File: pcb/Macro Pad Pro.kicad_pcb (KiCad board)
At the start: 4 copper layers, 107 x 134 mm, 150 parts, among them J1 USB_C, J2 Conn_02x08_Odd_Even, J3 Conn_02x01, J4 Conn_02x01, SW1 SW_Push_B, SW2 SW_Push_R, U1 RP2040, U3 AP2112K-3.3, U4 USBLC6-2SC6, U6 W25Q128JVS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

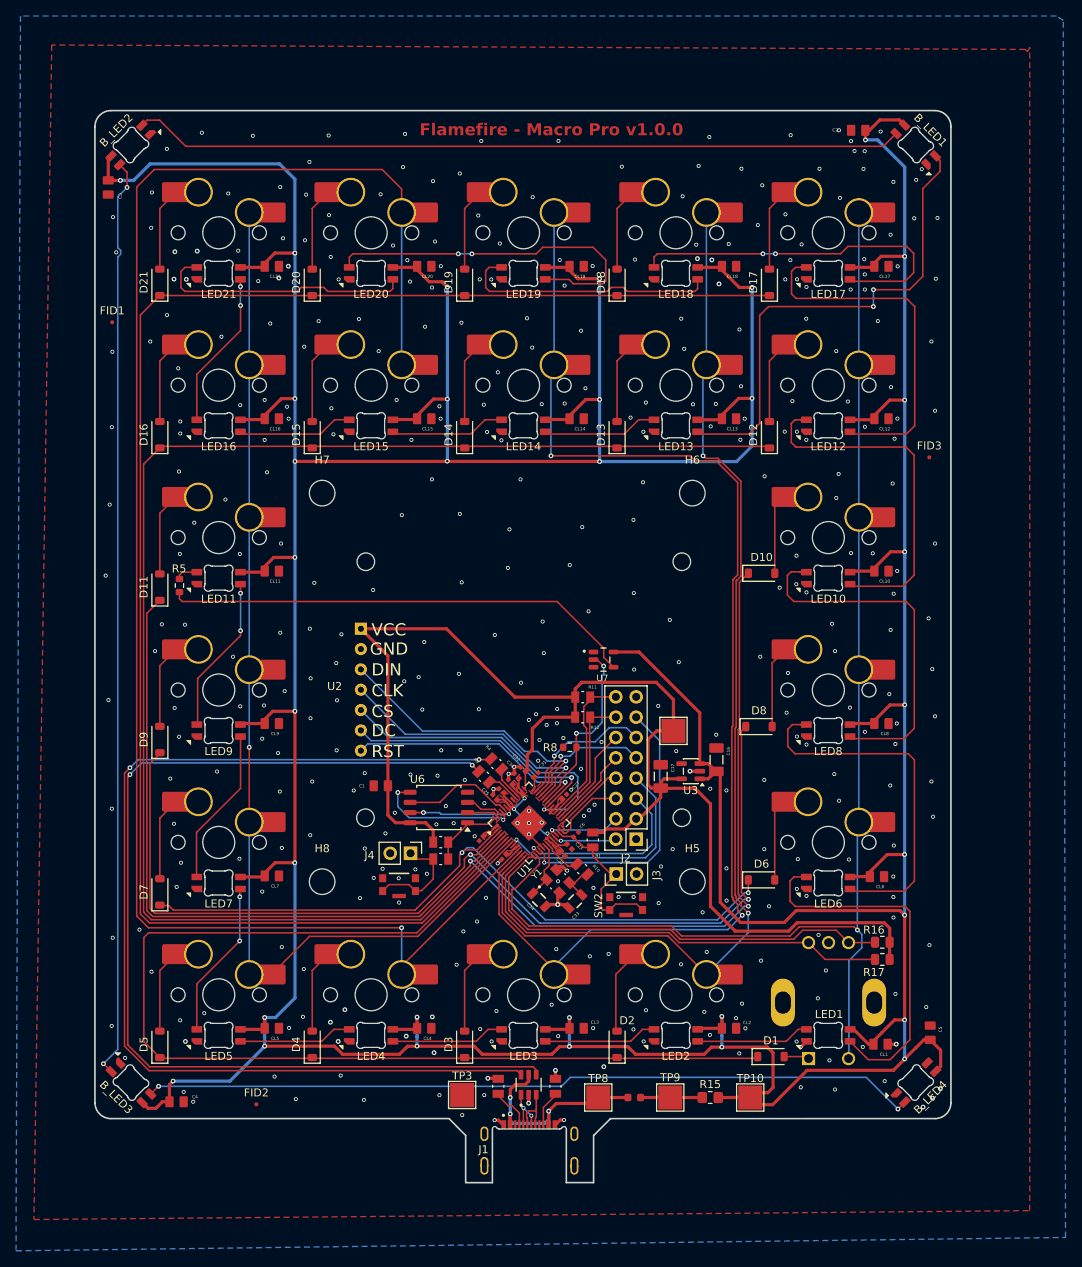
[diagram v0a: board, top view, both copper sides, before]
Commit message: cleaned up BOM and updated most components with LCSC number and MPN, sent to PCBWay for review
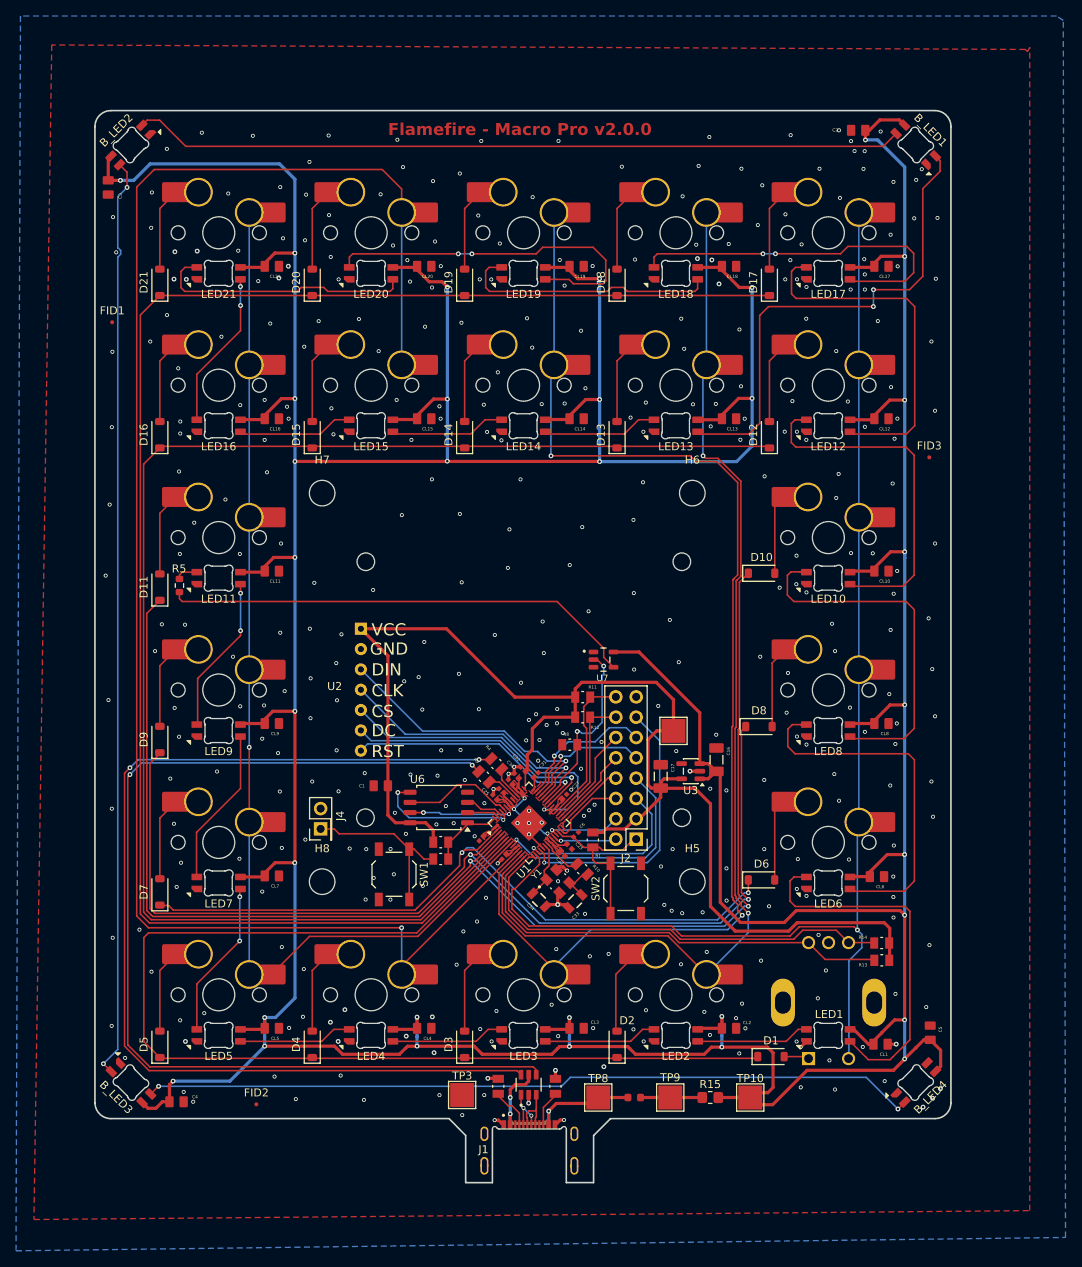
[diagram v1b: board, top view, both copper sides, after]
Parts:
- removed J3: Conn_02x01, Connector_PinHeader_2.54mm:PinHeader_1x02_P2.54mm_Vertical
- removed R16, R17: 10k, Resistor_SMD:R_0805_2012Metric
- added R13: 10k, Personal:10k_RESC2012X65N, F.Cu at (139.8, 154.7)
- added R14: 10k, Personal:10k_RESC2012X65N, F.Cu at (139.8, 152.5)
- J4: footprint Connector_PinHeader_2.54mm:PinHeader_1x02_P2.54mm_Vertical -> Connector_PinHeader_2.54mm:PinHeader_2x01_P2.54mm_Vertical
- R5: value 500 ohm -> 470 ohm
- R8: value 500 ohm -> 10k; footprint Resistor_SMD:R_0603_1608Metric -> Personal:10k_RESC2012X65N
- SW1, SW2: footprint Personal:SW_KMR221GLFS -> Button_Switch_SMD:SW_SPST_TL3342
- U1: footprint Personal:QFN-56-1EP_7x7mm_P0.4mm_EP3.2x3.2mm -> Package_DFN_QFN:QFN-56-1EP_7x7mm_P0.4mm_EP3.2x3.2mm
- U2: value ~ -> OLED
- moved J4 11.6 mm to (69.7, 138.2), turned to 90 degrees
- moved SW2 1.89 mm to (107.8, 145.7), turned to 90 degrees
- moved SW1 1.44 mm to (78.9, 143.9), turned to -90 degrees
- moved R8 0.32 mm to (100.8, 127.7)
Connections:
- J2 pad 1: unconnected-(J2-Pin_1-Pad1) -> NRST
- J2 pad 15: unconnected-(J2-Pin_15-Pad15) -> GND
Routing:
- net BOOTSEL: track 13.2 -> 21.9 mm
- net NRST: track 21.0 -> 21.6 mm
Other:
- copper layers 4 -> 2
- board text added: "Flamefire - Macro Pro v2.0.0"
- board text removed: "Flamefire - Macro Pro v1.0.0"
